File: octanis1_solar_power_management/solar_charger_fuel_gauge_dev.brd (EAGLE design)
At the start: 75 x 47.4 mm, 109 parts, among them IC401 TUSB2046BIRHBIRHB, Q2 32.768kHz, Q4 CSTCR4M00G15L99, Q401 CSTCR6M00G15L99, T1 BC547, T2 BC547, U1 BQ24210, U2 BQ27510_DRZ_12, U3 DRV8836DSSR, U4 DRV8836DSSR, U402 TPS62237DRY, U404 TPD2E001DRLR, U5 DRV8836DSSR, U6 MSP430F5529IPNR, U7 DRV8836DSSR

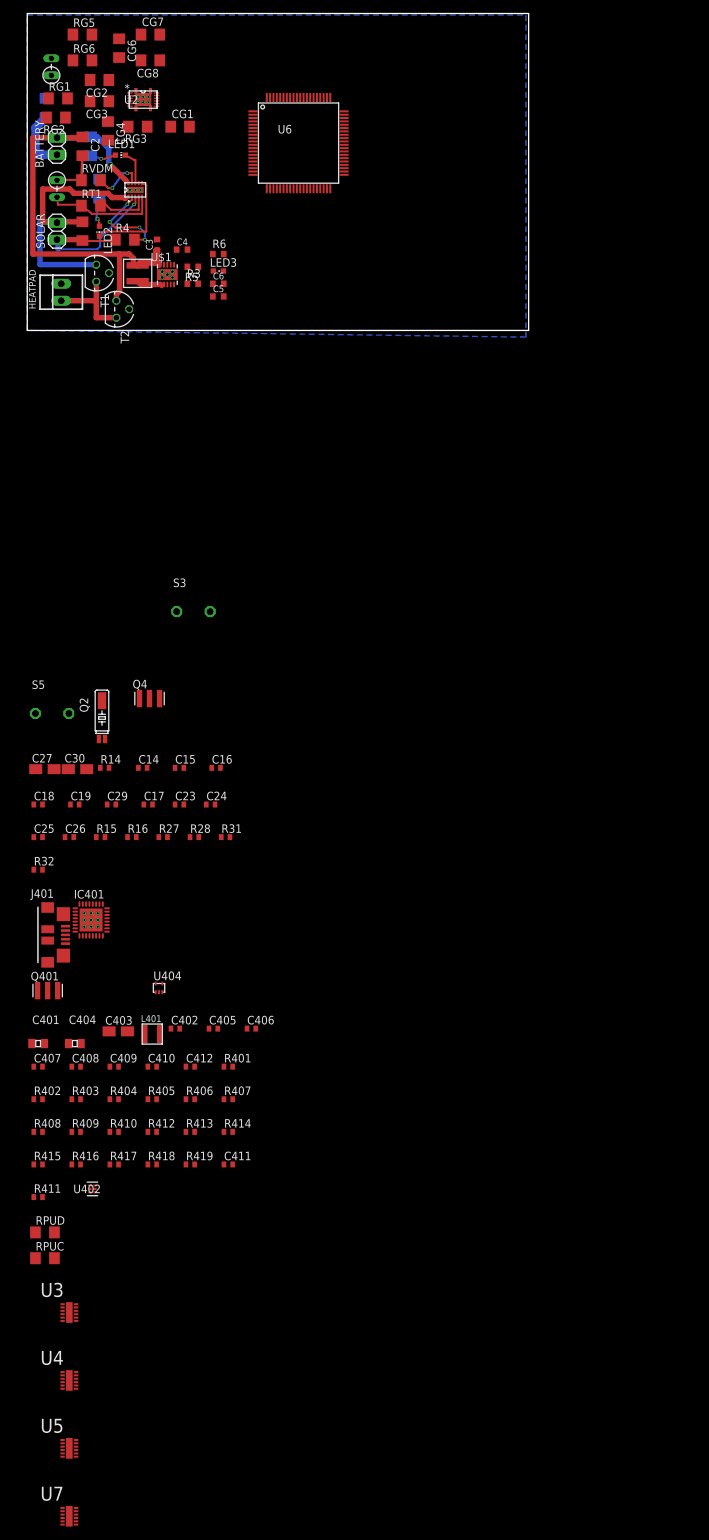
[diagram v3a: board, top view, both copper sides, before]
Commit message: arranged power components and h-bridges
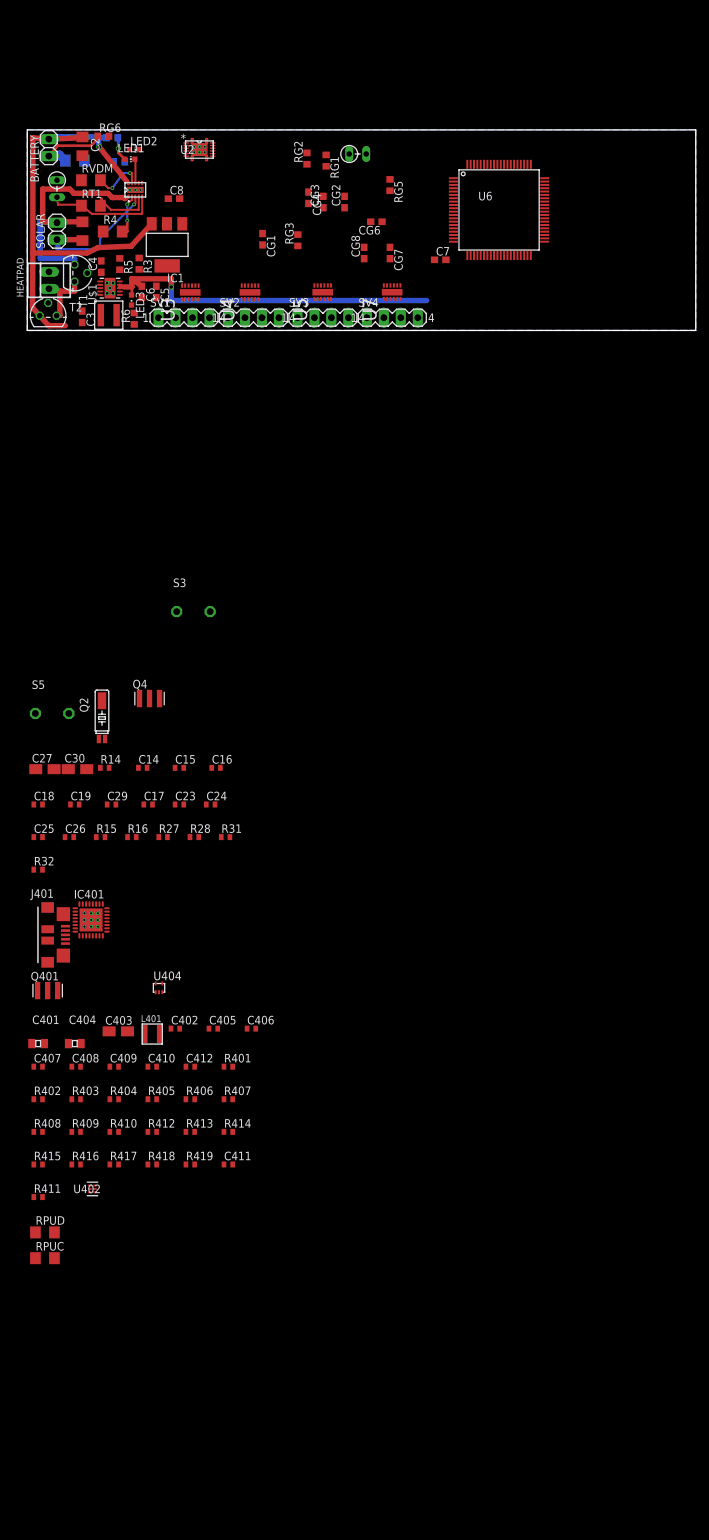
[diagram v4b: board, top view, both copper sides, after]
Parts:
- added C7, C8: 1uF, rcl:C0603
- added IC1: REG1117, burr-brown:SOT223
- added SV1, SV2, SV3, SV4: (no value), con-lstb:MA04-1
- C3, C4, C5, C6: device adafruit:C0603K -> rcl:C0603
- CG1, CG2, CG3, CG4, CG6, CG7, CG8: device rcl:C1206 -> rcl:C0603
- R1, R2, RG1, RG2, RG3, RG5, RG6: device resistor:R1206 -> rcl:R0603
- R3, R5, R6: device adafruit:R0603 -> rcl:R0603
- moved U7 189.4 mm to (54.6, 5.71), turned to 90 degrees
- moved U5 177.1 mm to (44.2, 5.71), turned to 90 degrees
- moved U4 165.0 mm to (33.3, 5.69), turned to 90 degrees
- moved U3 153.7 mm to (24.4, 5.69), turned to 90 degrees
- moved RG5 51.2 mm to (54.3, 21.7), turned to 270 degrees
- moved CG7 48.5 mm to (54.3, 11.6), turned to 270 degrees
- moved TEMP2 47.6 mm to (49.4, 26.4), turned to 0 degrees
- moved CG6 46.4 mm to (52.2, 16.3), turned to 180 degrees
- moved CG8 43.0 mm to (50.4, 11.6), turned to 90 degrees
- moved RG1 41.2 mm to (44.7, 25.4), turned to 270 degrees
- moved CG2 41.0 mm to (47.5, 19.2), turned to 90 degrees
- moved RG2 38.0 mm to (41.8, 25.7), turned to 90 degrees
- moved CG3 36.7 mm to (44.3, 19.2), turned to 90 degrees
- moved CG4 31.6 mm to (42.1, 19.8)
- moved U6 31.6 mm to (70.6, 18.0)
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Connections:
- removed net 5V: C5.1, C6.1, LED3.A, R3.2, U$1.3, U$1.4
- new net +3V3: C14.1, C19.2, C30.+, C8.1, IC1.2, R27.2, R28.2, RPUC.2, RPUD.2, S5.1, U6.18, U6.50
- new net M12MODE: U3.11
- new net M12SLEEP: U3.12
- new net M1IN1: U3.10
- new net M1IN2: U3.9
- new net M2IN1: U3.8
- new net M2IN2: U3.7
- new net M34MODE: U4.11
- new net M34SLEEP: U4.12
- new net M3IN1: U4.10
- new net M3IN2: U4.9
- new net M4IN1: U4.8
- new net M4IN2: U4.7
- new net M56MODE: U5.11
- new net M56SLEEP: U5.12
- new net M5IN1: U5.10
- new net M5IN2: U5.9
- new net M6IN1: U5.8
- new net M6IN2: U5.7
- new net M78MODE: U7.11
- new net M78SLEEP: U7.12
- new net M7IN1: U7.10
- new net M7IN2: U7.9
- new net M8IN1: U7.8
- new net M8IN2: U7.7
- new net N$13: SV2.1, U4.2
- new net N$39: SV2.2, U4.3
- new net N$40: SV2.3, U4.4
- new net N$41: SV2.4, U4.5
- new net N$45: SV3.1, U5.2
- new net N$46: SV3.2, U5.3
- new net N$47: SV3.3, U5.4
- new net N$48: SV3.4, U5.5
- new net N$49: SV1.1, U3.2
- new net N$50: SV1.2, U3.3
- new net N$51: SV1.3, U3.4
- new net N$52: SV1.4, U3.5
- new net N$53: SV4.1, U7.2
- new net N$54: SV4.2, U7.3
- new net N$55: SV4.3, U7.4
- new net N$56: SV4.4, U7.5
- net +5V: now also C5.1, C6.1, LED3.A, R3.2, U$1.3, U$1.4, U3.1, U4.1, U5.1, U7.1
- net BAT+: now also C7.1, IC1.3; no longer U3.1, U4.1, U5.1, U7.1
- net GND: now also C7.2, C8.2, IC1.1, U3.13, U3.6, U4.13, U4.6, U5.13, U5.6, U7.13, U7.6
- net SOLAR+: no longer C14.1, C19.2, C30.+, R27.2, R28.2, RPUC.2, RPUD.2, S5.1, U6.18, U6.50
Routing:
- net +5V: track 0.00 -> 54.0 mm, vias 0 -> 1
- net N$5: track 15.0 -> 0.00 mm
- net GND: track 34.7 -> 22.4 mm
- net N$10: track 13.7 -> 6.27 mm, vias 4 -> 2
- net N$3: track 5.32 -> 0.00 mm, vias 1 -> 0
- net IND: track 4.60 -> 0.00 mm
- net BAT+: track 72.0 -> 76.5 mm
- net N$37: track 13.7 -> 9.41 mm
- net SOLAR+: track 46.6 -> 43.2 mm
- net BAT-: track 9.46 -> 11.7 mm
- net N$4: track 5.16 -> 3.83 mm
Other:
- board size 75 x 47.4 mm -> 100 x 30 mm

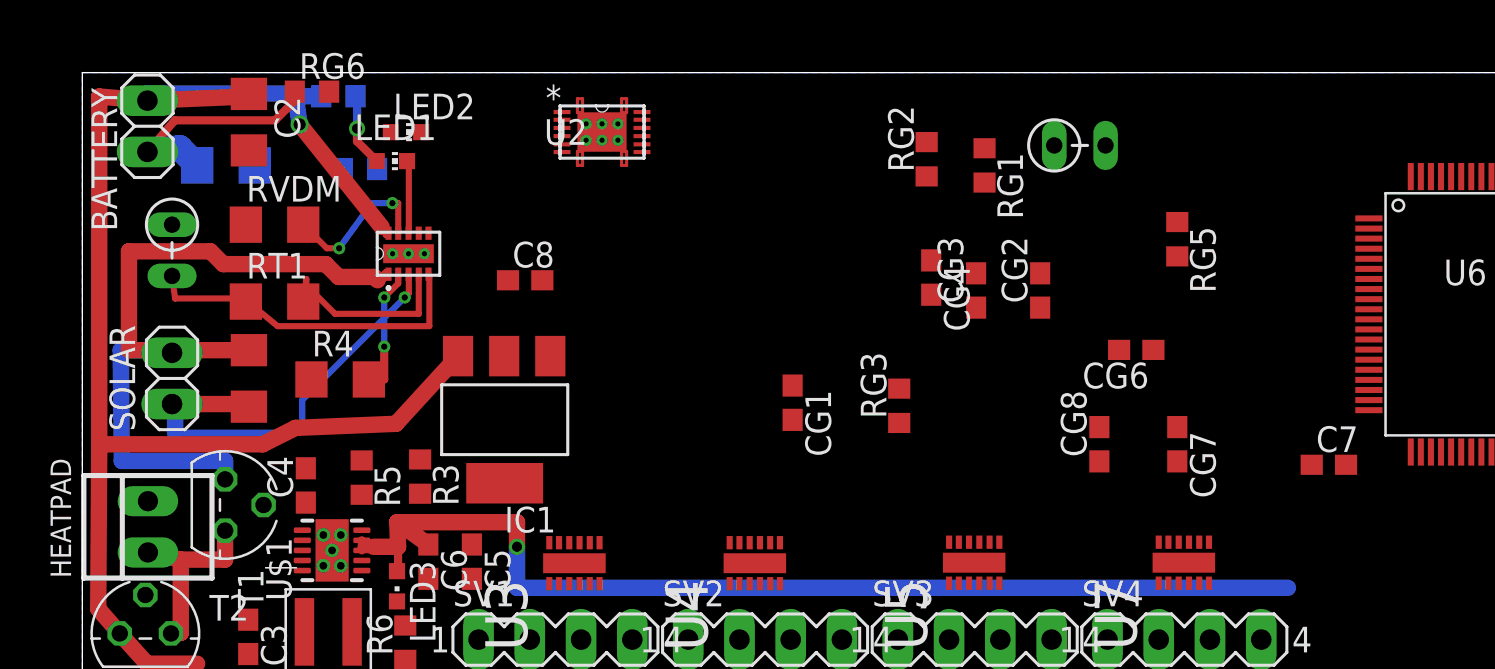
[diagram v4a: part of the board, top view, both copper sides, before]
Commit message: rearranged and routed fuel gauge circuit part
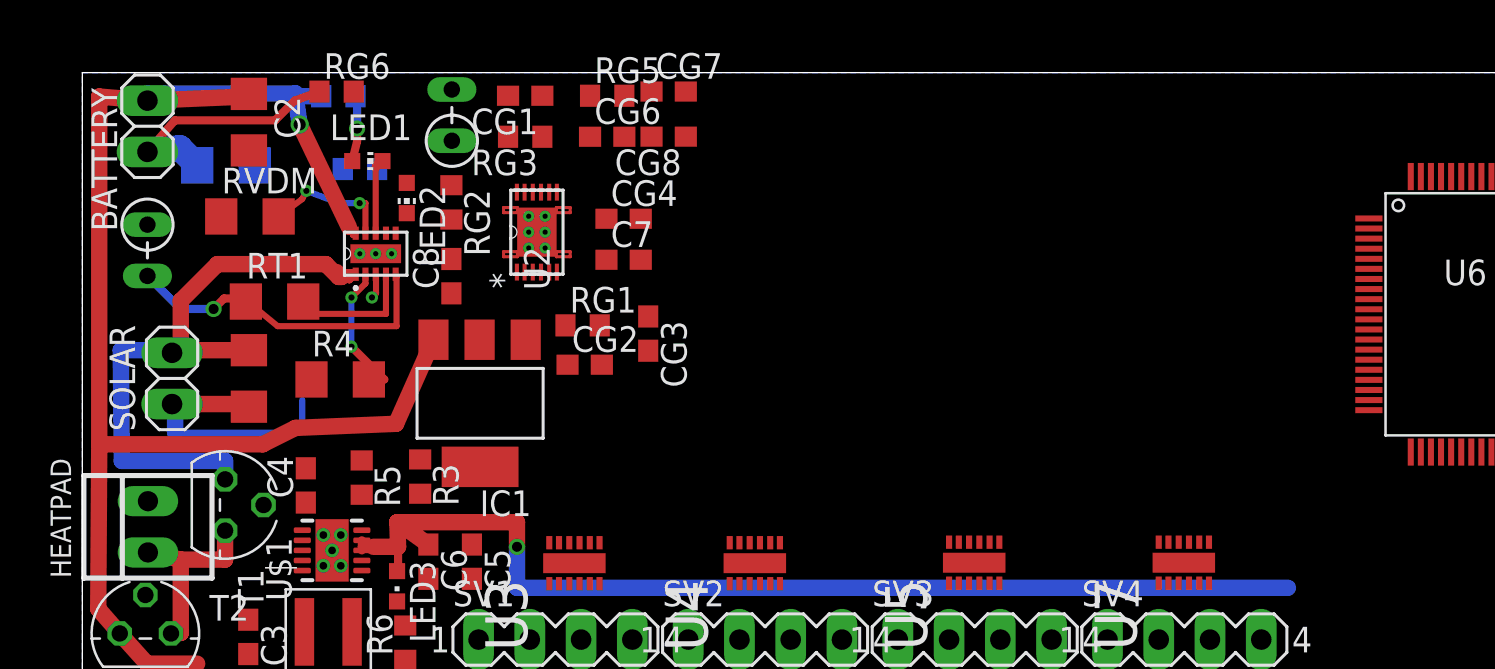
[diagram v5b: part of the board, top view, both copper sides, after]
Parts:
- moved C7 36.4 mm to (26.8, 20.7)
- moved TEMP2 31.2 mm to (18.3, 27.9), turned to 90 degrees
- moved CG7 30.7 mm to (29.1, 29.1), turned to 0 degrees
- moved RG5 29.1 mm to (26.0, 28.9), turned to 0 degrees
- moved CG6 28.3 mm to (26.0, 26.8), turned to 0 degrees
- moved CG8 26.2 mm to (29.1, 26.8), turned to 180 degrees
- moved RG2 23.6 mm to (18.3, 23.6), turned to 270 degrees
- moved CG2 22.9 mm to (24.9, 15.5), turned to 0 degrees
- moved RG3 22.8 mm to (21.9, 26.8), turned to 180 degrees
- moved RG1 21.4 mm to (24.8, 17.5), turned to 0 degrees
- moved CG1 20.2 mm to (21.9, 28.9), turned to 180 degrees
- moved CG3 16.4 mm to (28.0, 17.1), turned to 270 degrees
- moved CG4 15.5 mm to (26.8, 22.8), turned to 0 degrees
- moved U2 5.92 mm to (22.5, 22.1), turned to 90 degrees
- moved C8 3.66 mm to (18.3, 19.9), turned to 90 degrees
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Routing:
- net SOLAR+: track 43.2 -> 35.7 mm
- net GND: track 22.4 -> 15.2 mm
- net N$8: track 9.56 -> 6.32 mm
- net N$6: track 7.82 -> 6.44 mm
- net BAT+: track 76.5 -> 75.6 mm
- net BAT-: track 11.7 -> 12.6 mm
- net N$10: track 6.27 -> 6.94 mm
- net N$7: track 16.8 -> 16.4 mm, vias 0 -> 1

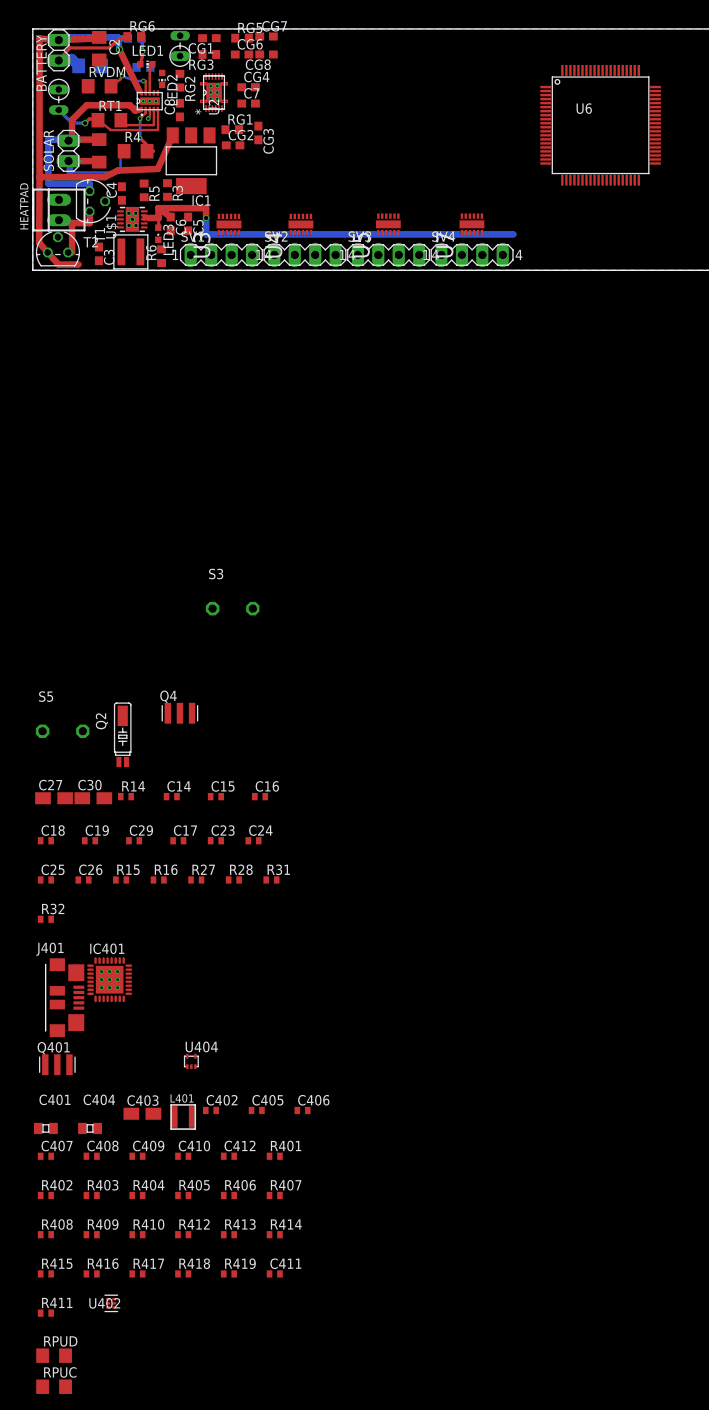
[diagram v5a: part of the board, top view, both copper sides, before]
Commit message: connected h-bridges to pins
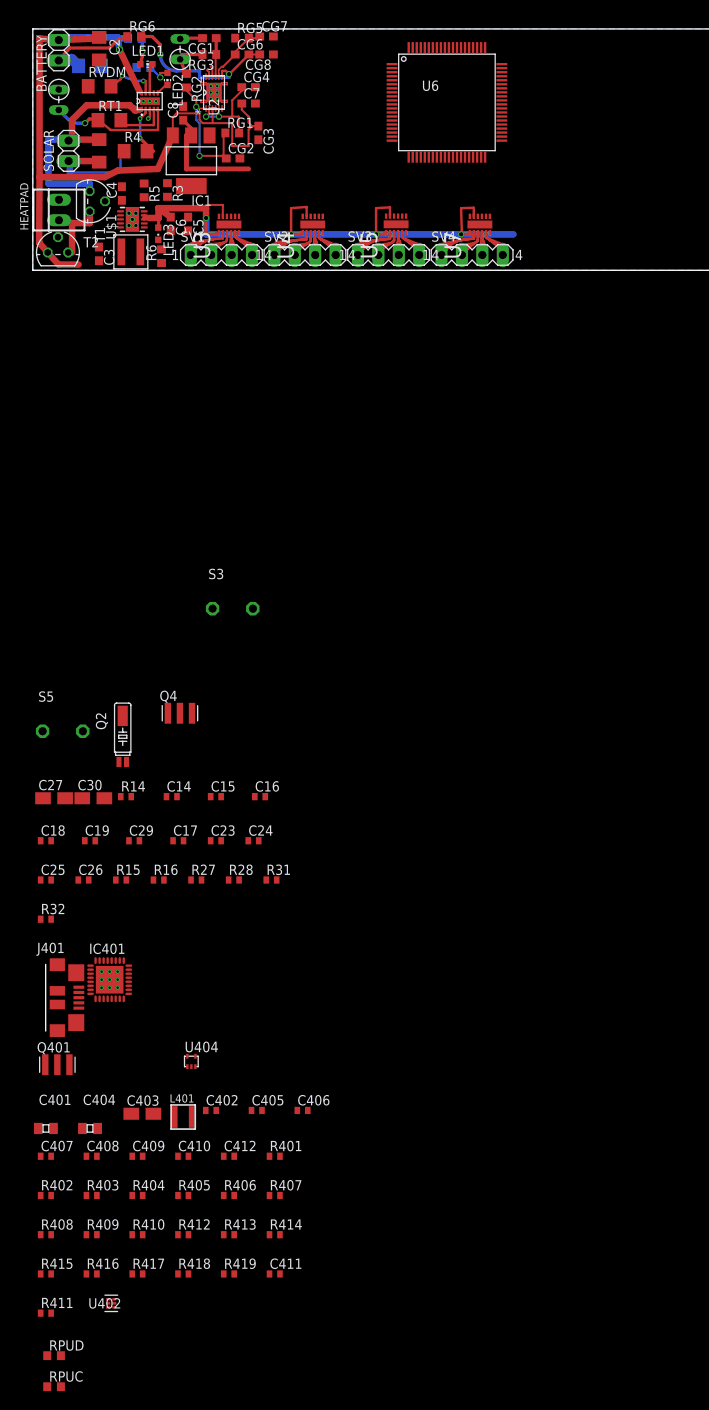
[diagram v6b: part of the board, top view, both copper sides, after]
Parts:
- RPUC, RPUD: device resistor:R1206 -> rcl:R0603
- moved U6 19.3 mm to (51.5, 20.9)
- moved CG2 1.63 mm to (24.9, 13.9)
- moved U4 1.47 mm to (34.8, 5.69)
- moved U7 0.99 mm to (55.6, 5.69)
- moved U5 0.97 mm to (45.2, 5.71)
- moved RG2 0.81 mm to (19.1, 23.6)
- moved LED2 0.66 mm to (16.7, 23.8)
- moved C8 0.57 mm to (18.7, 19.5)
- moved RG1 0.41 mm to (24.8, 17.1)
- moved TEMP2 0.41 mm to (18.3, 27.5)
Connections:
- removed net M12MODE: U3.11
- removed net M34MODE: U4.11
- removed net M56MODE: U5.11
- removed net M78MODE: U7.11
- net +5V: now also U3.11, U4.11, U5.11, U7.11
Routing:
- net +5V: track 54.0 -> 84.1 mm, vias 1 -> 4
- net BAT+: track 75.6 -> 100.5 mm
- net N$38: track 0.00 -> 21.2 mm, vias 0 -> 2
- net N$1: track 0.00 -> 17.0 mm, vias 0 -> 2
- net N$49: track 0.00 -> 15.5 mm
- net N$58: track 0.00 -> 15.5 mm
- net N$63: track 0.00 -> 15.5 mm
- net N$68: track 0.00 -> 15.5 mm
- net +3V3: track 0.00 -> 14.8 mm
- net N$35: track 0.00 -> 12.4 mm, vias 0 -> 2
- net N$52: track 0.00 -> 8.90 mm
- net N$61: track 0.00 -> 8.90 mm
- net N$71: track 0.00 -> 8.90 mm
- net N$66: track 0.00 -> 8.90 mm
- net N$51: track 0.00 -> 8.17 mm
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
